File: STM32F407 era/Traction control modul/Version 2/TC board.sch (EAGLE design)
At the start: 89 parts, among them IC1 74HC14D, IC2 lm2575, IC3 74AC08D, IC5 REG1117, IC6 74AC14D, J1 CON1, J2 CON1, Q5 IRFR3707ZR, Q8 IRFR3707ZR, U1 MAX13052ESA+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

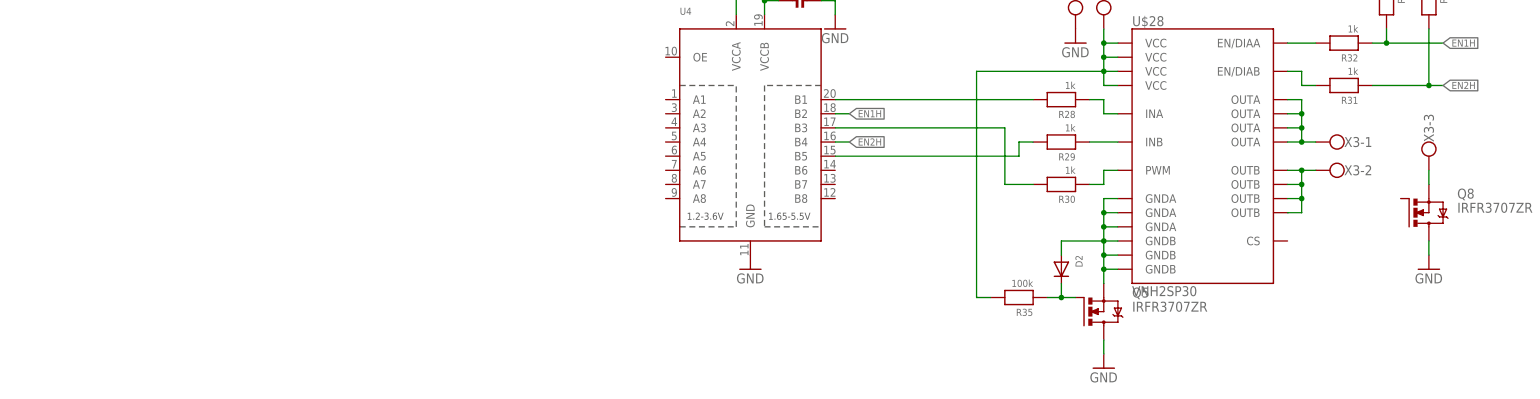
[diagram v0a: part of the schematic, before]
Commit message: more work on h-bridge layout
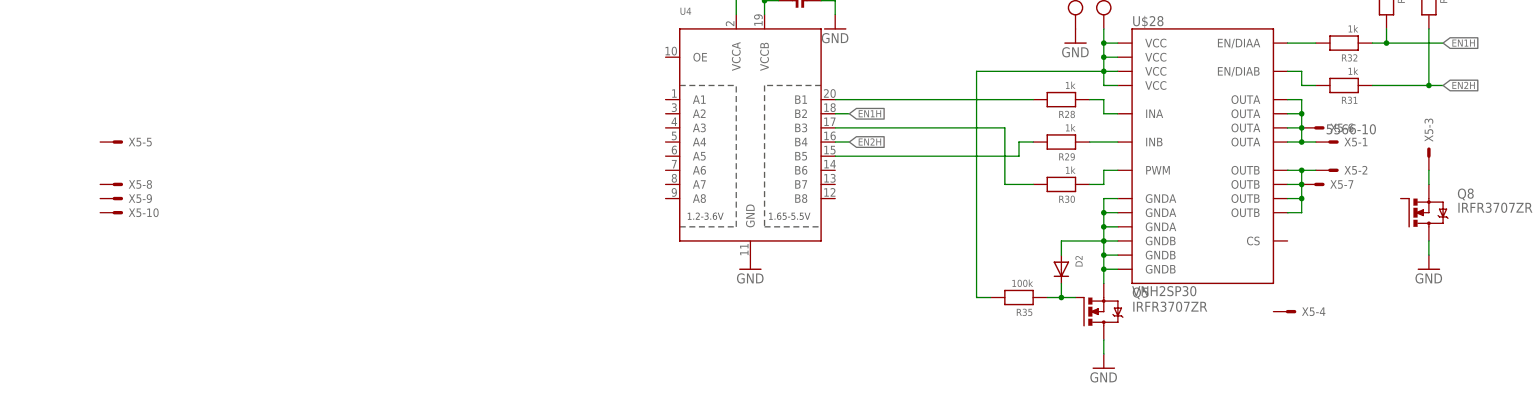
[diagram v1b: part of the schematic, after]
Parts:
- removed X3: (no value), con-wago-500:W237-103
- added X5: 5566-10, con-molex:5566-10
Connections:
- removed net N$27: U$28.OUTA@1, U$28.OUTA@25, U$28.OUTA@30, U$28.OUTA@SLUG3, X3-1.KL
- removed net N$37: U$28.OUTB@15, U$28.OUTB@16, U$28.OUTB@21, U$28.OUTB@SLUG2, X3-2.KL
- new net OUTA: U$28.OUTA@1, U$28.OUTA@25, U$28.OUTA@30, U$28.OUTA@SLUG3, X5-1.S, X5-6.S
- new net OUTB: U$28.OUTB@15, U$28.OUTB@16, U$28.OUTB@21, U$28.OUTB@SLUG2, X5-2.S, X5-7.S
- net MP: now also X5-3.S; no longer X3-3.KL
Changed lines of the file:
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@@
 <part name="R21" library="microbuilder" deviceset="RESISTOR" device="_0603" value="221"/>
 <part name="X2" library="con-wago-500" deviceset="W237-102" device=""/>
-<part name="X3" library="con-wago-500" deviceset="W237-103" device=""/>
 <part name="GND27" library="supply1" deviceset="GND" device=""/>
 <part name="R28" library="microbuilder" deviceset="RESISTOR" device="_0603" value="1k"/>
@@
 <part name="GND44" library="supply1" deviceset="GND" device=""/>
 <part name="C6" library="microbuilder" deviceset="CAP_CERAMIC" device="_0603" value="100n"/>
+<part name="X5" library="con-molex" deviceset="5566-10" device=""/>
 </parts>
 <sheets>
@@
 <instance part="X2" gate="-1" x="236.22" y="-12.7" rot="R270"/>
 <instance part="X2" gate="-2" x="231.14" y="-12.7" rot="R270"/>
-<instance part="X3" gate="-1" x="279.4" y="-38.1" rot="R180"/>
-<instance part="X3" gate="-2" x="279.4" y="-43.18" rot="R180"/>
-<instance part="X3" gate="-3" x="294.64" y="-38.1" rot="R270"/>
 <instance part="GND27" gate="1" x="236.22" y="-78.74"/>
 <instance part="R28" gate="G$1" x="228.6" y="-30.48" rot="R180"/>
@@
 <instance part="GND44" gate="1" x="187.96" y="-17.78"/>
 <instance part="C6" gate="G$1" x="180.34" y="-12.7" rot="MR90"/>
+<instance part="X5" gate="-1" x="276.86" y="-38.1"/>
+<instance part="X5" gate="-2" x="276.86" y="-43.18"/>
+<instance part="X5" gate="-3" x="294.64" y="-40.64" rot="R90"/>
+<instance part="X5" gate="-4" x="269.24" y="-68.58"/>
+<instance part="X5" gate="-5" x="58.42" y="-38.1"/>
+<instance part="X5" gate="-6" x="274.32" y="-35.56"/>
+<instance part="X5" gate="-7" x="274.32" y="-45.72"/>
+<instance part="X5" gate="-8" x="58.42" y="-45.72"/>
+<instance part="X5" gate="-9" x="58.42" y="-48.26"/>
+<instance part="X5" gate="-10" x="58.42" y="-50.8"/>
 </instances>
 <busses>
@@
 </segment>
 </net>
-<net name="N$27" class="0">
+<net name="OUTA" class="0">
 <segment>
 <pinref part="U$28" gate="G$1" pin="OUTA@1"/>
-<pinref part="X3" gate="-1" pin="KL"/>
-<wire x1="274.32" y1="-38.1" x2="271.78" y2="-38.1" width="0.1524" layer="91"/>
 <pinref part="U$28" gate="G$1" pin="OUTA@25"/>
 <wire x1="271.78" y1="-38.1" x2="269.24" y2="-38.1" width="0.1524" layer="91"/>
 <wire x1="269.24" y1="-35.56" x2="271.78" y2="-35.56" width="0.1524" layer="91"/>
 <wire x1="271.78" y1="-35.56" x2="271.78" y2="-38.1" width="0.1524" layer="91"/>
-<junction x="271.78" y="-38.1"/>
 <pinref part="U$28" gate="G$1" pin="OUTA@30"/>
 <wire x1="269.24" y1="-33.02" x2="271.78" y2="-33.02" width="0.1524" layer="91"/>
@@
 <wire x1="271.78" y1="-30.48" x2="271.78" y2="-33.02" width="0.1524" layer="91"/>
 <junction x="271.78" y="-33.02"/>
-</segment>
-</net>
-<net name="N$37" class="0">
+<pinref part="X5" gate="-1" pin="S"/>
+<wire x1="274.32" y1="-38.1" x2="271.78" y2="-38.1" width="0.1524" layer="91"/>
+<junction x="271.78" y="-38.1"/>
+<pinref part="X5" gate="-6" pin="S"/>
+</segment>
+</net>
+<net name="OUTB" class="0">
 <segment>
 <pinref part="U$28" gate="G$1" pin="OUTB@15"/>
 <wire x1="271.78" y1="-50.8" x2="269.24" y2="-50.8" width="0.1524" layer="91"/>
 <pinref part="U$28" gate="G$1" pin="OUTB@SLUG2"/>
-<pinref part="X3" gate="-2" pin="KL"/>
-<wire x1="274.32" y1="-43.18" x2="271.78" y2="-43.18" width="0.1524" layer="91"/>
 <pinref part="U$28" gate="G$1" pin="OUTB@21"/>
 <wire x1="271.78" y1="-43.18" x2="269.24" y2="-43.18" width="0.1524" layer="91"/>
 <wire x1="269.24" y1="-45.72" x2="271.78" y2="-45.72" width="0.1524" layer="91"/>
 <wire x1="271.78" y1="-45.72" x2="271.78" y2="-43.18" width="0.1524" layer="91"/>
-<junction x="271.78" y="-43.18"/>
 <pinref part="U$28" gate="G$1" pin="OUTB@16"/>
 <wire x1="269.24" y1="-48.26" x2="271.78" y2="-48.26" width="0.1524" layer="91"/>
@@
 <wire x1="271.78" y1="-50.8" x2="271.78" y2="-48.26" width="0.1524" layer="91"/>
 <junction x="271.78" y="-48.26"/>
+<pinref part="X5" gate="-2" pin="S"/>
+<wire x1="274.32" y1="-43.18" x2="271.78" y2="-43.18" width="0.1524" layer="91"/>
+<junction x="271.78" y="-43.18"/>
+<pinref part="X5" gate="-7" pin="S"/>
 </segment>
 </net>
@@
 <segment>
 <pinref part="Q8" gate="G$1" pin="S"/>
-<pinref part="X3" gate="-3" pin="KL"/>
 <wire x1="294.64" y1="-43.18" x2="294.64" y2="-45.72" width="0.1524" layer="91"/>
-</segment>
-</net>
+<pinref part="X5" gate="-3" pin="S"/>
+</segment>
+</net>

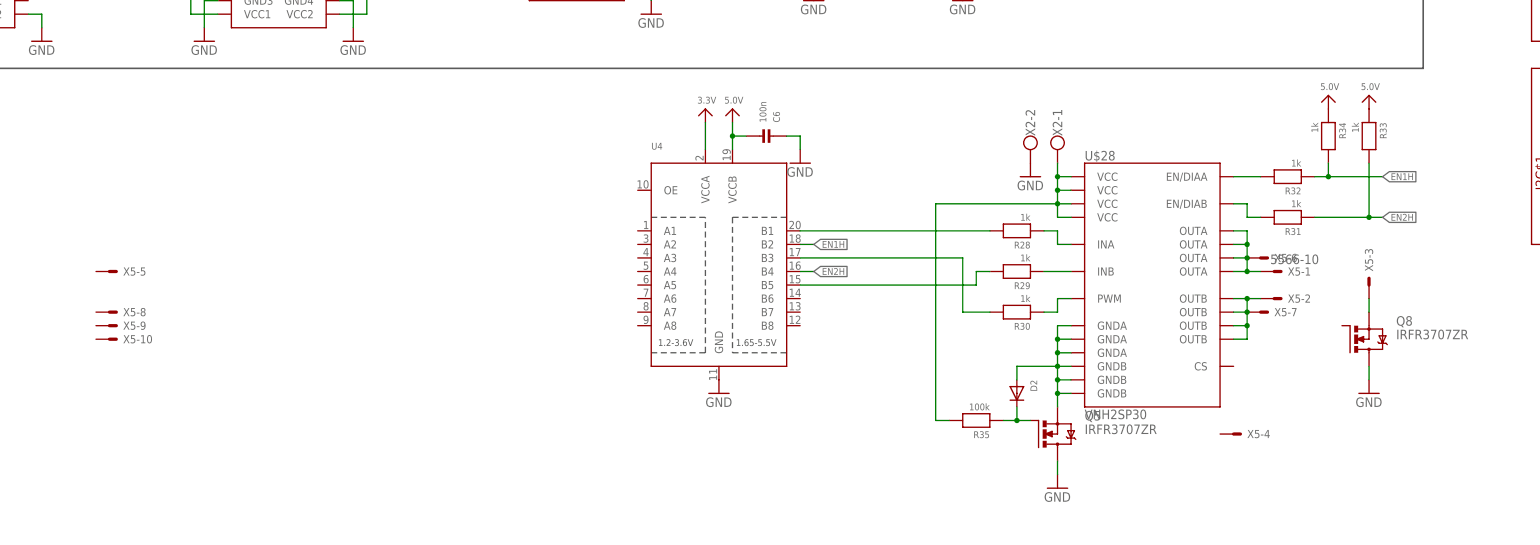
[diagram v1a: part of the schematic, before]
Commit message: more work on TC, first layout of 3G test board
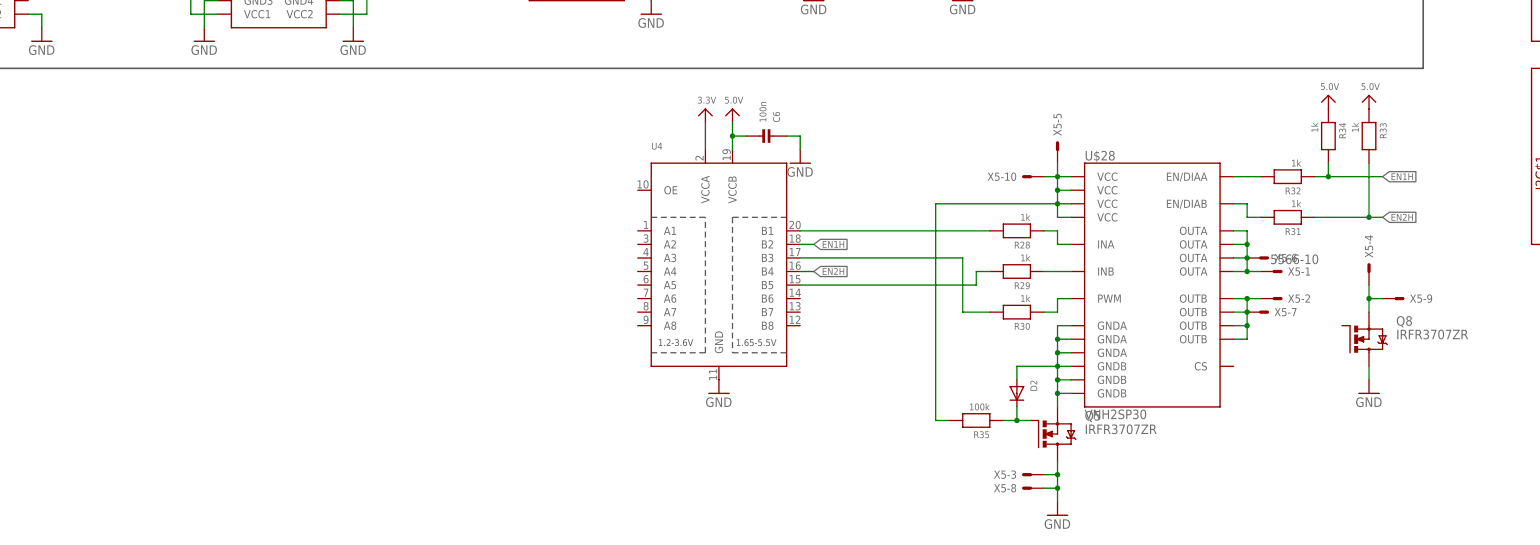
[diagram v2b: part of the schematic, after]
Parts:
- removed X2: (no value), con-wago-500:W237-102
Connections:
- net OUTB renamed CVVM
- removed net MP: Q8.S, X5-3.S
- removed net N$53: R35.2, U$28.VCC@13, U$28.VCC@23, U$28.VCC@3, U$28.VCC@SLUG1, X2-1.KL
- new net GNDM: Q8.S, X5-4.S, X5-9.S
- new net VCCM: R35.2, U$28.VCC@13, U$28.VCC@23, U$28.VCC@3, U$28.VCC@SLUG1, X5-10.S, X5-5.S
- net GND: now also X5-3.S, X5-8.S; no longer X2-2.KL
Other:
- moved on the sheet: X5-10, X5-3, X5-4, X5-5, X5-8, X5-9
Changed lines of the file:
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@@
 <part name="R20" library="microbuilder" deviceset="RESISTOR" device="_0603" value="221"/>
 <part name="R21" library="microbuilder" deviceset="RESISTOR" device="_0603" value="221"/>
-<part name="X2" library="con-wago-500" deviceset="W237-102" device=""/>
 <part name="GND27" library="supply1" deviceset="GND" device=""/>
 <part name="R28" library="microbuilder" deviceset="RESISTOR" device="_0603" value="1k"/>
@@
 <part name="Q8" library="UNICORN" deviceset="IRFR3707Z" device="R"/>
 <part name="GND41" library="supply1" deviceset="GND" device=""/>
-<part name="GND42" library="supply1" deviceset="GND" device=""/>
 <part name="U4" library="adafruit" deviceset="TXB0108PWR" device=""/>
 <part name="U$29" library="microbuilder" deviceset="5.0V" device=""/>
@@
 <instance part="R20" gate="G$1" x="294.64" y="180.34" rot="R90"/>
 <instance part="R21" gate="G$1" x="307.34" y="180.34" rot="R90"/>
-<instance part="X2" gate="-1" x="236.22" y="-12.7" rot="R270"/>
-<instance part="X2" gate="-2" x="231.14" y="-12.7" rot="R270"/>
-<instance part="GND27" gate="1" x="236.22" y="-78.74"/>
+<instance part="GND27" gate="1" x="236.22" y="-83.82"/>
 <instance part="R28" gate="G$1" x="228.6" y="-30.48" rot="R180"/>
 <instance part="R29" gate="G$1" x="228.6" y="-38.1" rot="R180"/>
@@
 <instance part="Q8" gate="G$1" x="292.1" y="-50.8"/>
 <instance part="GND41" gate="1" x="294.64" y="-60.96"/>
-<instance part="GND42" gate="1" x="231.14" y="-20.32"/>
 <instance part="U4" gate="G$1" x="172.72" y="-35.56"/>
 <instance part="U$29" gate="G$1" x="175.26" y="-7.62"/>
@@
 <instance part="X5" gate="-1" x="276.86" y="-38.1"/>
 <instance part="X5" gate="-2" x="276.86" y="-43.18"/>
-<instance part="X5" gate="-3" x="294.64" y="-40.64" rot="R90"/>
-<instance part="X5" gate="-4" x="269.24" y="-68.58"/>
-<instance part="X5" gate="-5" x="58.42" y="-38.1"/>
+<instance part="X5" gate="-3" x="231.14" y="-76.2" rot="R180"/>
+<instance part="X5" gate="-4" x="294.64" y="-38.1" rot="R90"/>
+<instance part="X5" gate="-5" x="236.22" y="-15.24" rot="R90"/>
 <instance part="X5" gate="-6" x="274.32" y="-35.56"/>
 <instance part="X5" gate="-7" x="274.32" y="-45.72"/>
-<instance part="X5" gate="-8" x="58.42" y="-45.72"/>
-<instance part="X5" gate="-9" x="58.42" y="-48.26"/>
-<instance part="X5" gate="-10" x="58.42" y="-50.8"/>
+<instance part="X5" gate="-8" x="231.14" y="-78.74" rot="R180"/>
+<instance part="X5" gate="-9" x="299.72" y="-43.18"/>
+<instance part="X5" gate="-10" x="231.14" y="-20.32" rot="R180"/>
 </instances>
 <busses>
@@
 <pinref part="GND27" gate="1" pin="GND"/>
 <pinref part="Q5" gate="G$1" pin="D"/>
+<wire x1="236.22" y1="-81.28" x2="236.22" y2="-78.74" width="0.1524" layer="91"/>
+<pinref part="X5" gate="-3" pin="S"/>
+<wire x1="236.22" y1="-78.74" x2="236.22" y2="-76.2" width="0.1524" layer="91"/>
 <wire x1="236.22" y1="-76.2" x2="236.22" y2="-73.66" width="0.1524" layer="91"/>
+<wire x1="233.68" y1="-76.2" x2="236.22" y2="-76.2" width="0.1524" layer="91"/>
+<junction x="236.22" y="-76.2"/>
+<pinref part="X5" gate="-8" pin="S"/>
+<wire x1="236.22" y1="-78.74" x2="233.68" y2="-78.74" width="0.1524" layer="91"/>
+<junction x="236.22" y="-78.74"/>
 </segment>
 <segment>
@@
 <pinref part="GND41" gate="1" pin="GND"/>
 <wire x1="294.64" y1="-58.42" x2="294.64" y2="-55.88" width="0.1524" layer="91"/>
-</segment>
-<segment>
-<pinref part="X2" gate="-2" pin="KL"/>
-<pinref part="GND42" gate="1" pin="GND"/>
 </segment>
 <segment>
@@
 </segment>
 </net>
-<net name="OUTB" class="0">
+<net name="CVVM" class="0">
 <segment>
 <pinref part="U$28" gate="G$1" pin="OUTB@15"/>
@@
 </segment>
 </net>
-<net name="MP" class="0">
-<segment>
-<pinref part="Q8" gate="G$1" pin="S"/>
-<wire x1="294.64" y1="-43.18" x2="294.64" y2="-45.72" width="0.1524" layer="91"/>
-<pinref part="X5" gate="-3" pin="S"/>
-</segment>
-</net>
-<net name="N$53" class="0">
+<net name="VCCM" class="0">
 <segment>
 <pinref part="R35" gate="G$1" pin="2"/>
@@
 <pinref part="U$28" gate="G$1" pin="VCC@3"/>
 <wire x1="238.76" y1="-20.32" x2="236.22" y2="-20.32" width="0.1524" layer="91"/>
-<wire x1="236.22" y1="-20.32" x2="236.22" y2="-17.78" width="0.1524" layer="91"/>
 <pinref part="U$28" gate="G$1" pin="VCC@13"/>
 <wire x1="238.76" y1="-22.86" x2="236.22" y2="-22.86" width="0.1524" layer="91"/>
 <wire x1="236.22" y1="-22.86" x2="236.22" y2="-20.32" width="0.1524" layer="91"/>
-<junction x="236.22" y="-20.32"/>
 <pinref part="U$28" gate="G$1" pin="VCC@23"/>
 <wire x1="238.76" y1="-25.4" x2="236.22" y2="-25.4" width="0.1524" layer="91"/>
@@
 <wire x1="236.22" y1="-27.94" x2="236.22" y2="-25.4" width="0.1524" layer="91"/>
 <junction x="236.22" y="-25.4"/>
-<pinref part="X2" gate="-1" pin="KL"/>
 <wire x1="213.36" y1="-25.4" x2="236.22" y2="-25.4" width="0.1524" layer="91"/>
+<pinref part="X5" gate="-10" pin="S"/>
+<wire x1="233.68" y1="-20.32" x2="236.22" y2="-20.32" width="0.1524" layer="91"/>
+<junction x="236.22" y="-20.32"/>
+<pinref part="X5" gate="-5" pin="S"/>
+<wire x1="236.22" y1="-20.32" x2="236.22" y2="-17.78" width="0.1524" layer="91"/>
 </segment>
 </net>
@@
 </segment>
 </net>
+<net name="GNDM" class="0">
+<segment>
+<pinref part="Q8" gate="G$1" pin="S"/>
+<pinref part="X5" gate="-4" pin="S"/>
+<wire x1="294.64" y1="-40.64" x2="294.64" y2="-43.18" width="0.1524" layer="91"/>
+<pinref part="X5" gate="-9" pin="S"/>
+<wire x1="294.64" y1="-43.18" x2="294.64" y2="-45.72" width="0.1524" layer="91"/>
+<wire x1="294.64" y1="-43.18" x2="297.18" y2="-43.18" width="0.1524" layer="91"/>
+<junction x="294.64" y="-43.18"/>
+</segment>
+</net>
